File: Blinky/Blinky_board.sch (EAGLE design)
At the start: 11 parts, among them CN1 TORAGI-LPC-WRITER, U1 LPC810M021FN8

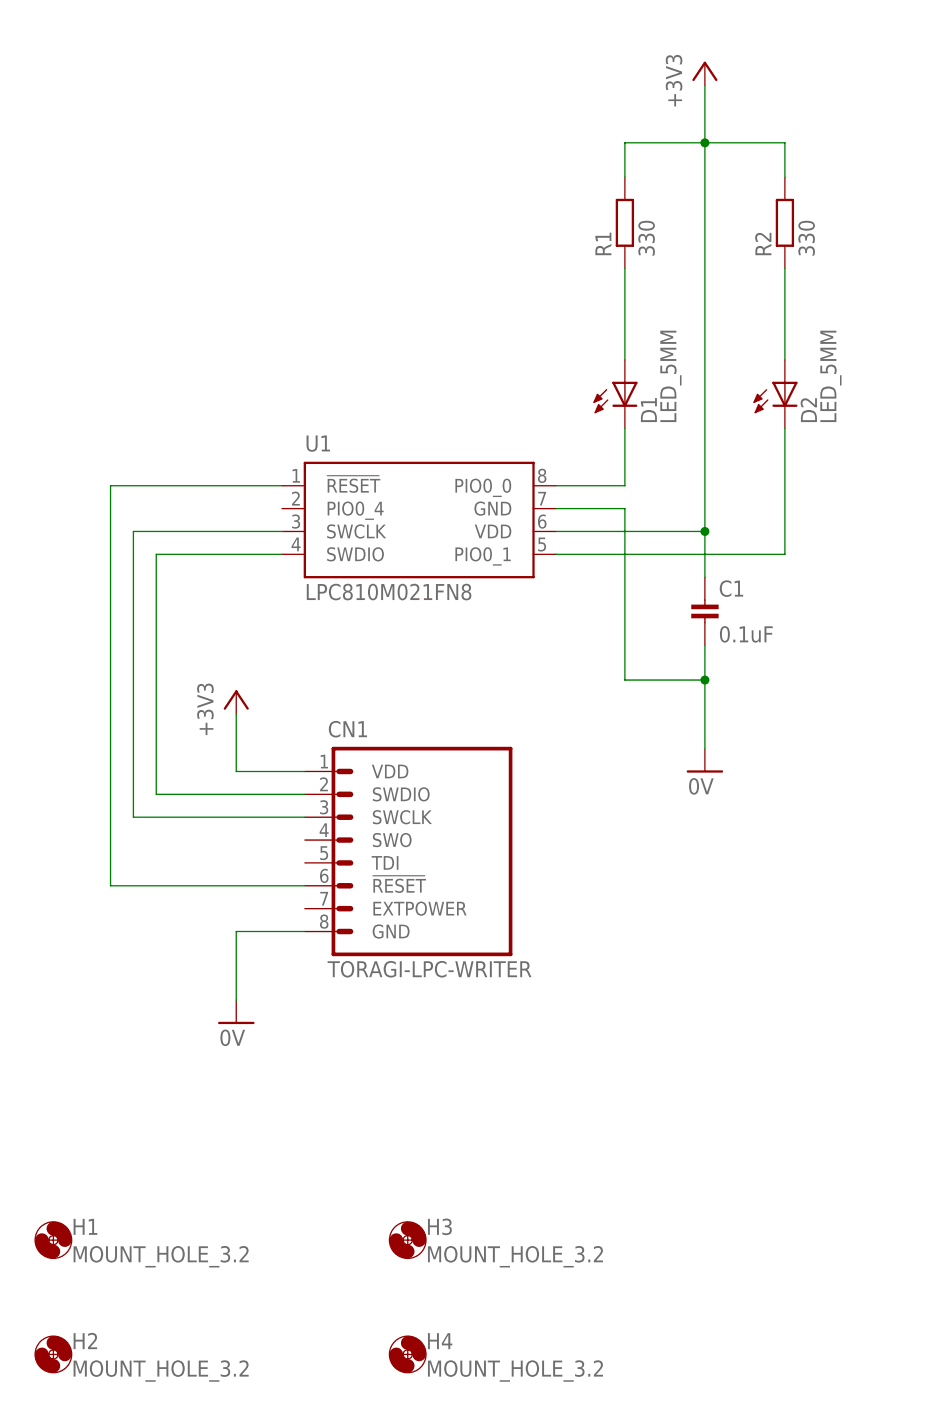
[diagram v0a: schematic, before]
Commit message: LPC810用サンプル回路（Blinky）修正
タクトスイッチを追加
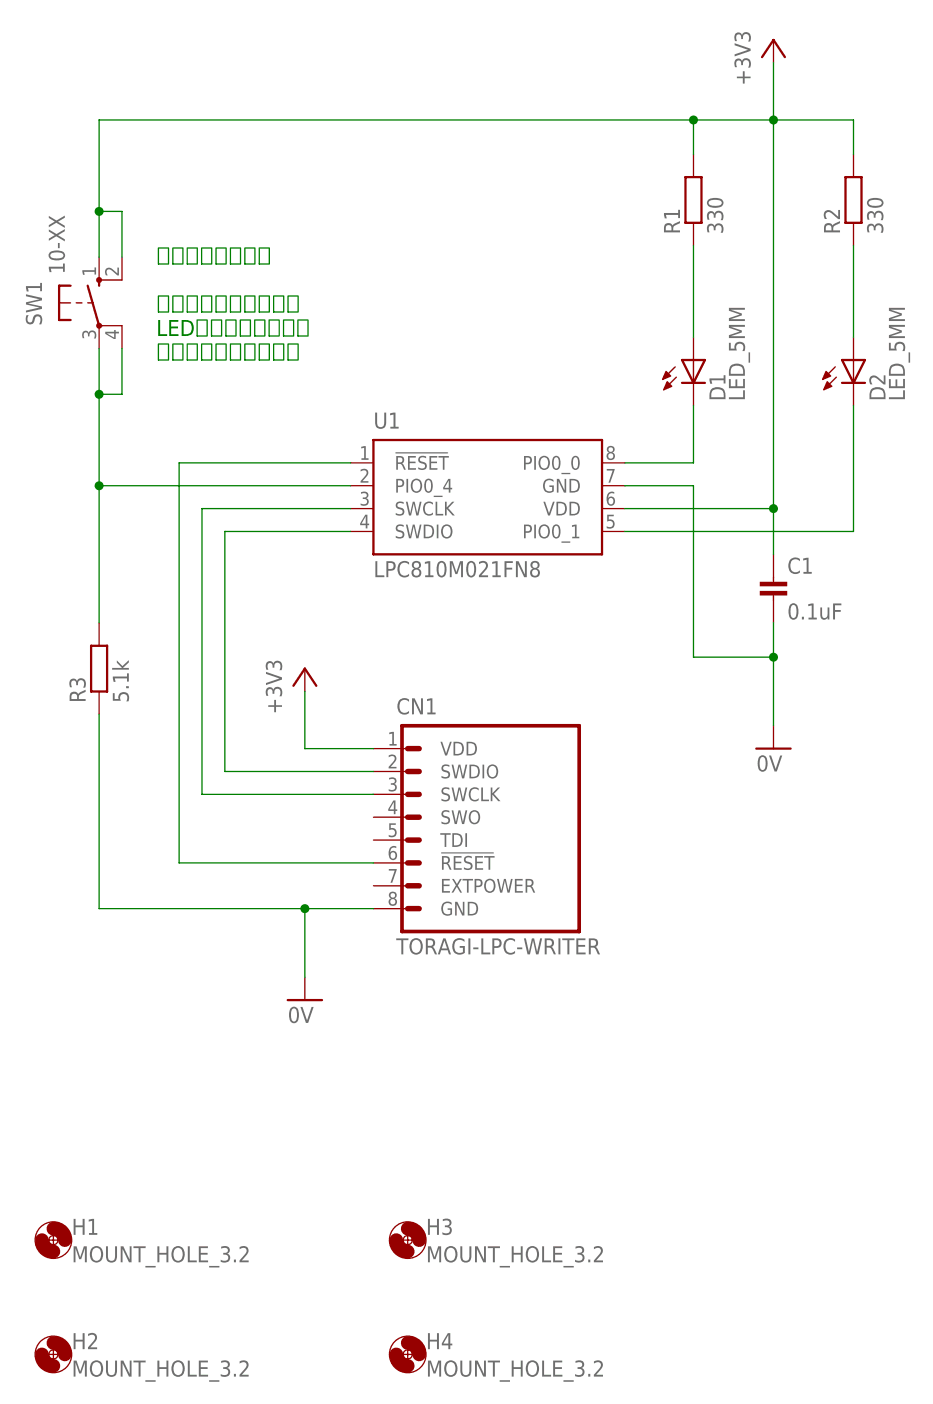
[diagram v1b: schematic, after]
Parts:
- added R3: 5.1k, Parts:RESISTOR_200MIL
- added SW1: 10-XX, Parts:10-XX
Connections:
- new net N$10: R3.2, SW1.P, SW1.P1, U1.PIO0_4
- net +3V3: now also SW1.S, SW1.S1
- net 0V: now also R3.1
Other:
- note added: "点滅切替スイッチ スイッチを押すたびに LED点滅をストップ／ リスタートさせます。"
- moved on the sheet: C1, CN1, D1, D2, R1, R2, U1
